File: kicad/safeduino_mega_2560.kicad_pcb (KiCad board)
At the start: 4 copper layers, 134.5 x 63.9 mm, 127 parts, among them X1 USB

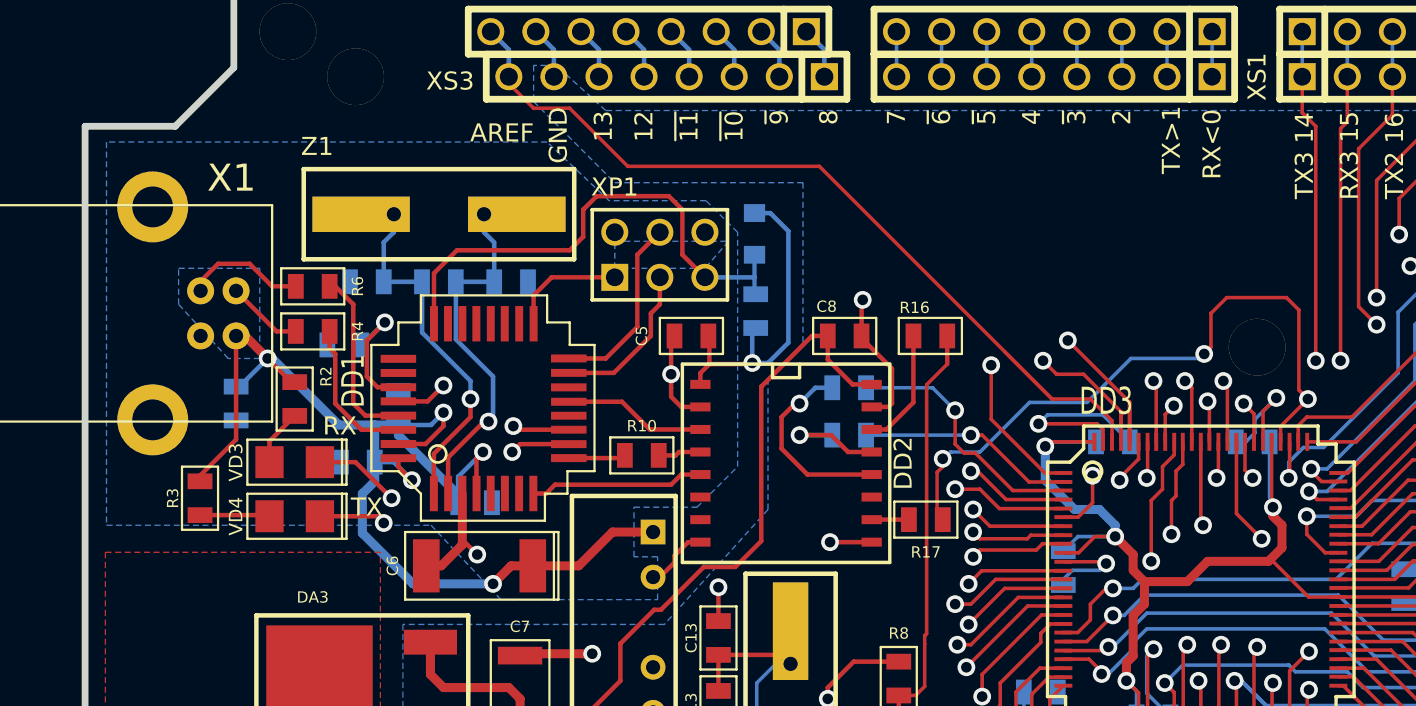
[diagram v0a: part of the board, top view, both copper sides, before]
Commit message: Исправил ошибку в подключении ADUM1301.
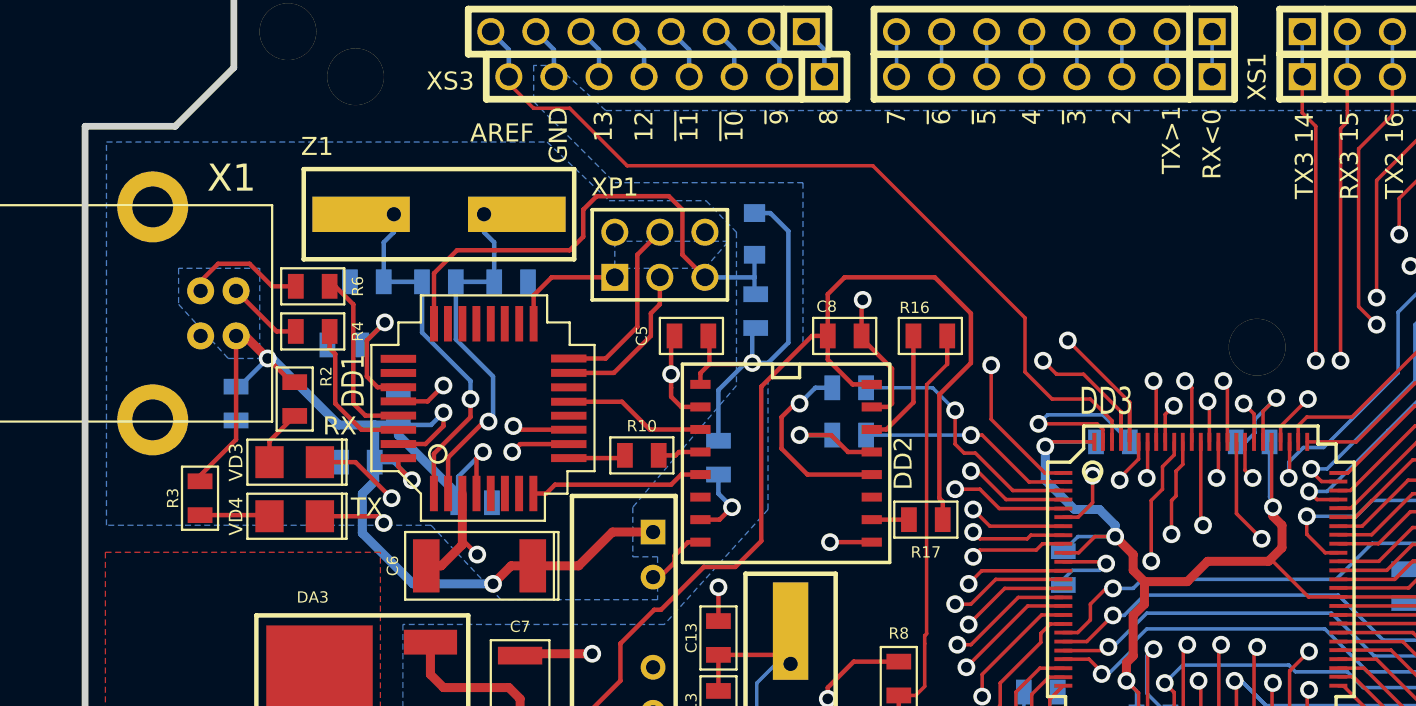
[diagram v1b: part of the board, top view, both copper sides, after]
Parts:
- added R19: 1к, SMD0805, B.Cu at (89.2, 118.1)
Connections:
- DD2 pad 7: (no net) -> N-0000037
- R17 pad 2: /PJ7 -> /MPU_VCC
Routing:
- net /PJ7: track 84.5 -> 50.2 mm, vias 4 -> 2
- net /MPU_VCC: track 434.4 -> 458.4 mm
- net /5V_USB: track 120.9 -> 126.3 mm
- net N-0000037: track 0.00 -> 4.22 mm, vias 0 -> 1
- net /AREF: track 50.2 -> 48.2 mm

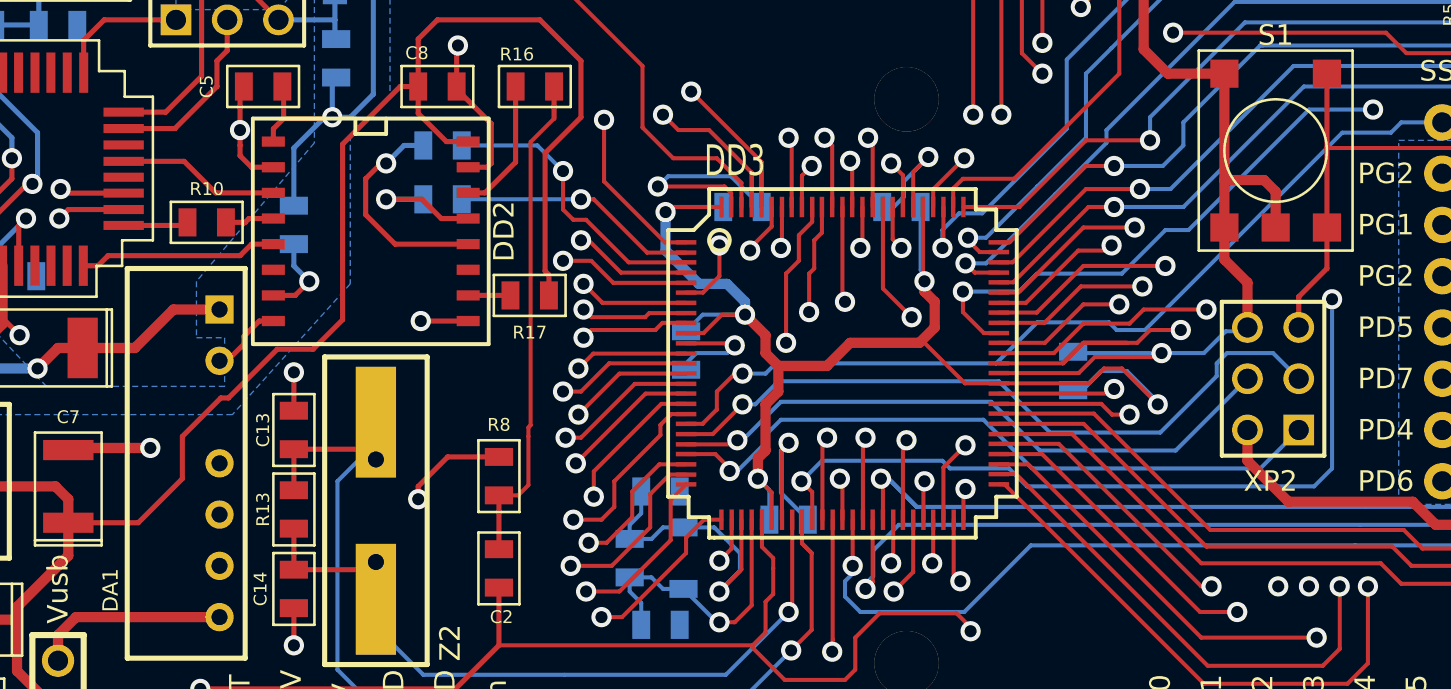
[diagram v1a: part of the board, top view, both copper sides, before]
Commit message: Исправил ошибку с сигналом RESER.
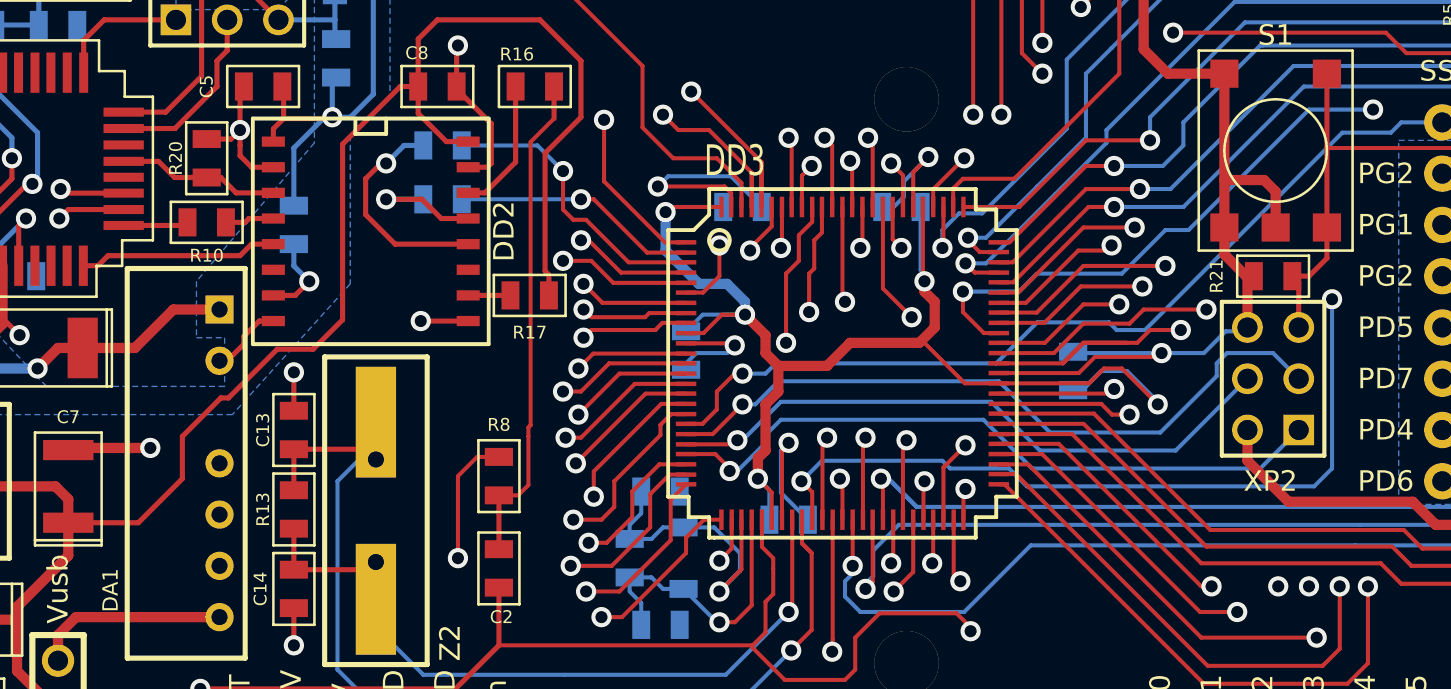
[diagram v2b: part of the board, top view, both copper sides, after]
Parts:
- added R20: 1к, SMD0805, F.Cu at (84.8, 114.8)
- added R21: 1М, SMD0805, F.Cu at (137.7, 120.7)
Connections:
- R8 pad 1: /GND_USB -> /GND
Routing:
- net /GND_USB: track 39.9 -> 23.0 mm, vias 4 -> 3
- net /GND: track 136.5 -> 143.7 mm, vias 14 -> 15
- net /RESET: track 116.1 -> 116.9 mm

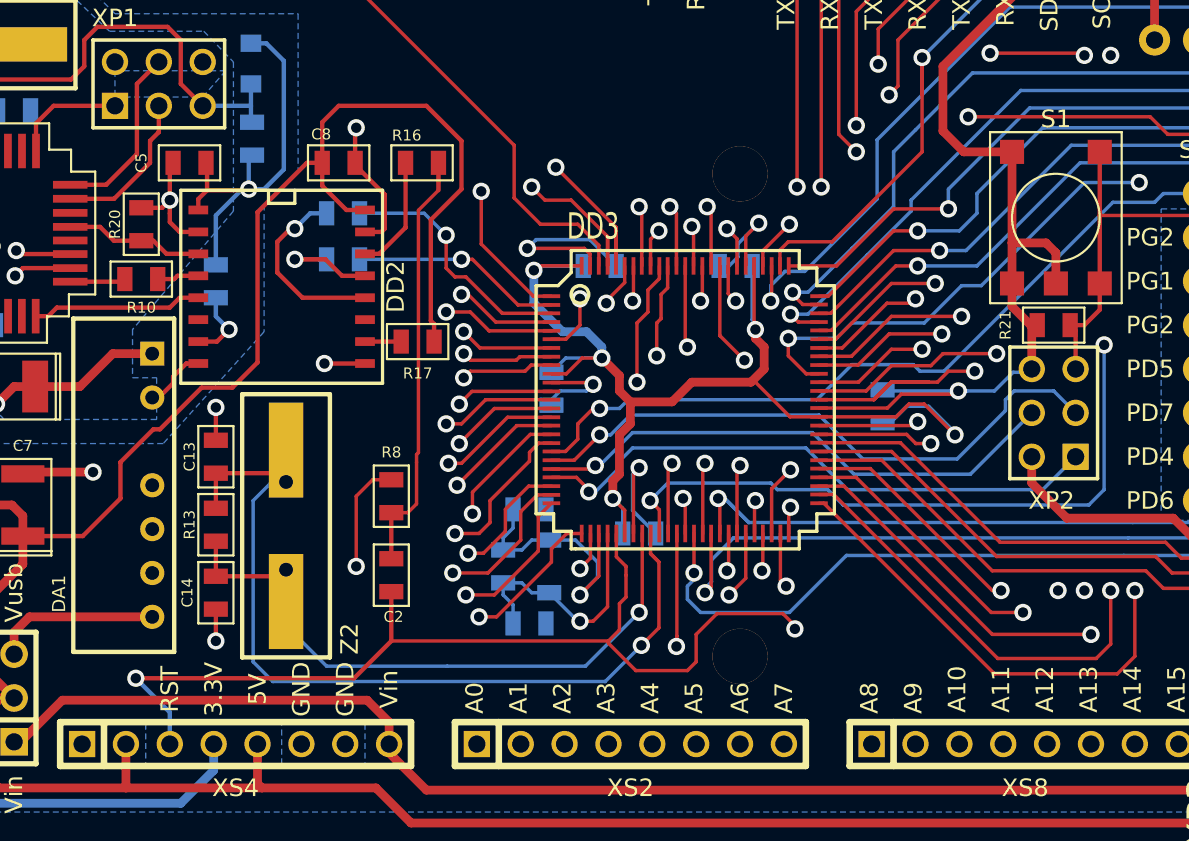
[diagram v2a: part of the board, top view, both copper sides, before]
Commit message: Услучшил разводку платы SafeDuino MEGA 2560.
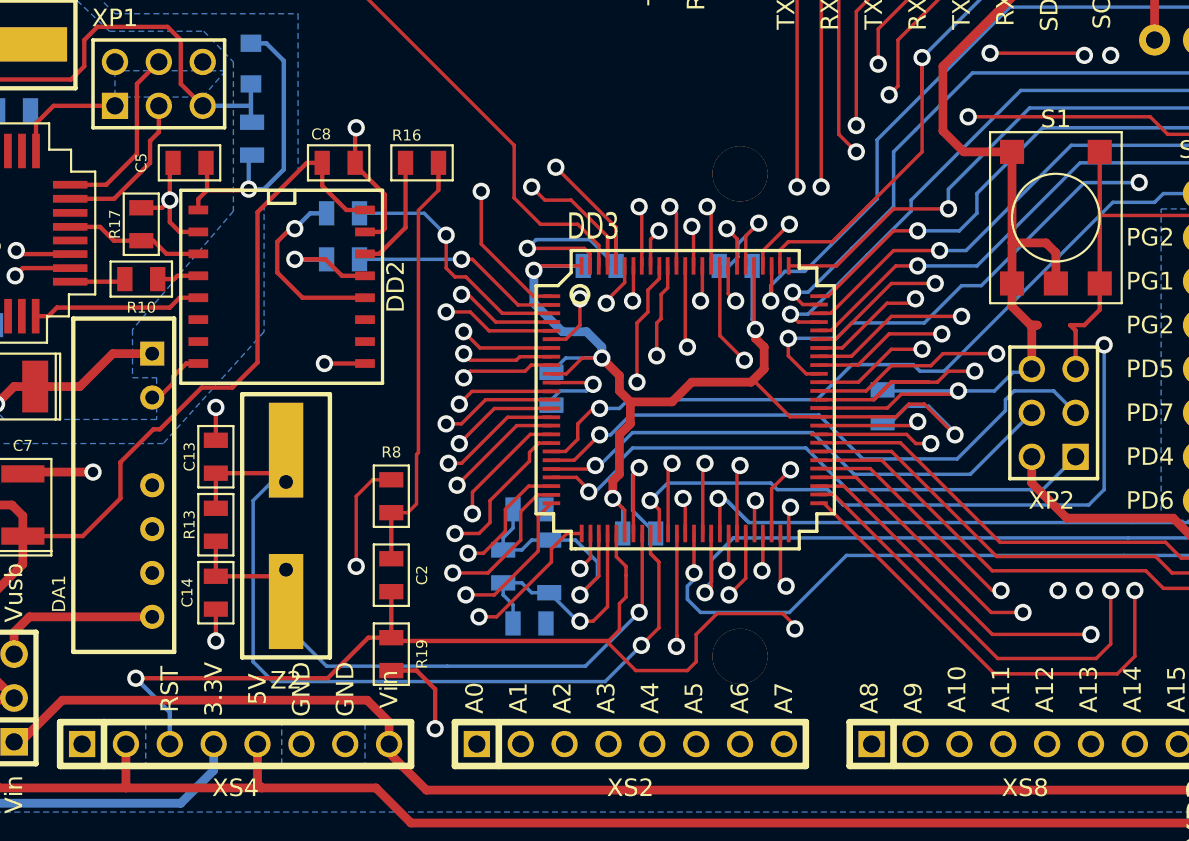
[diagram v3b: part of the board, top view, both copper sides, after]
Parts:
- removed the R17 at (100.8, 121.6)
- removed R21: 1М, SMD0805
- R19: value 1к -> 1М; moved to F.Cu
- moved R19 23.9 mm to (99.3, 139.7), turned to 90 degrees
- renumbered R20 to R17
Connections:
- DD2 pad 10: N-00000147 -> (no net)
- DD2 pad 7: N-0000048 -> (no net)
- R19 pad 1: /5V_USB -> /GND
- R19 pad 2: N-0000048 -> /RESET
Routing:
- net /MPU_VCC: track 458.4 -> 434.4 mm
- net /5V_USB: track 126.3 -> 120.9 mm
- net /GND: track 143.7 -> 149.0 mm, vias 15 -> 16
- net N-0000048: track 4.22 -> 0.00 mm, vias 1 -> 0
- net N-00000147: track 2.49 -> 0.00 mm

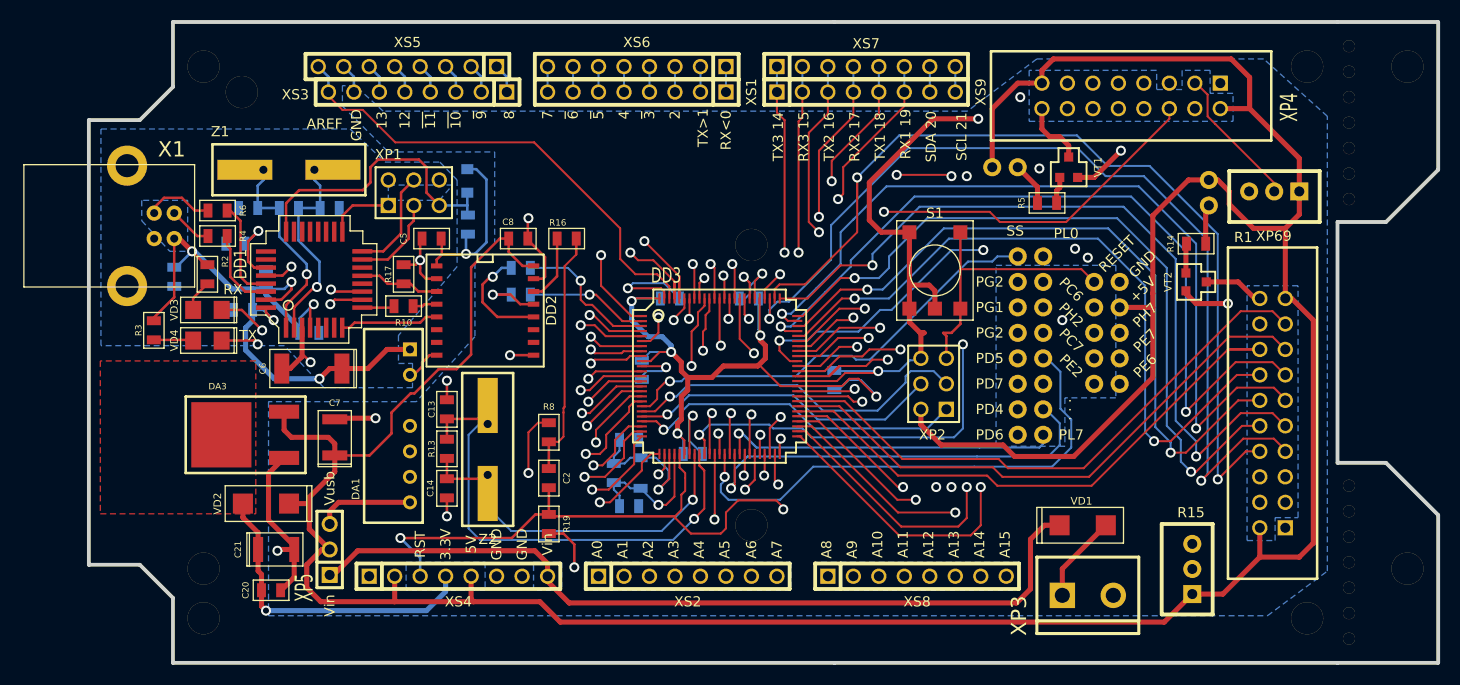
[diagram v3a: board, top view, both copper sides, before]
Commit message: Поправил ошибку с перевёрнутым разъёмом.
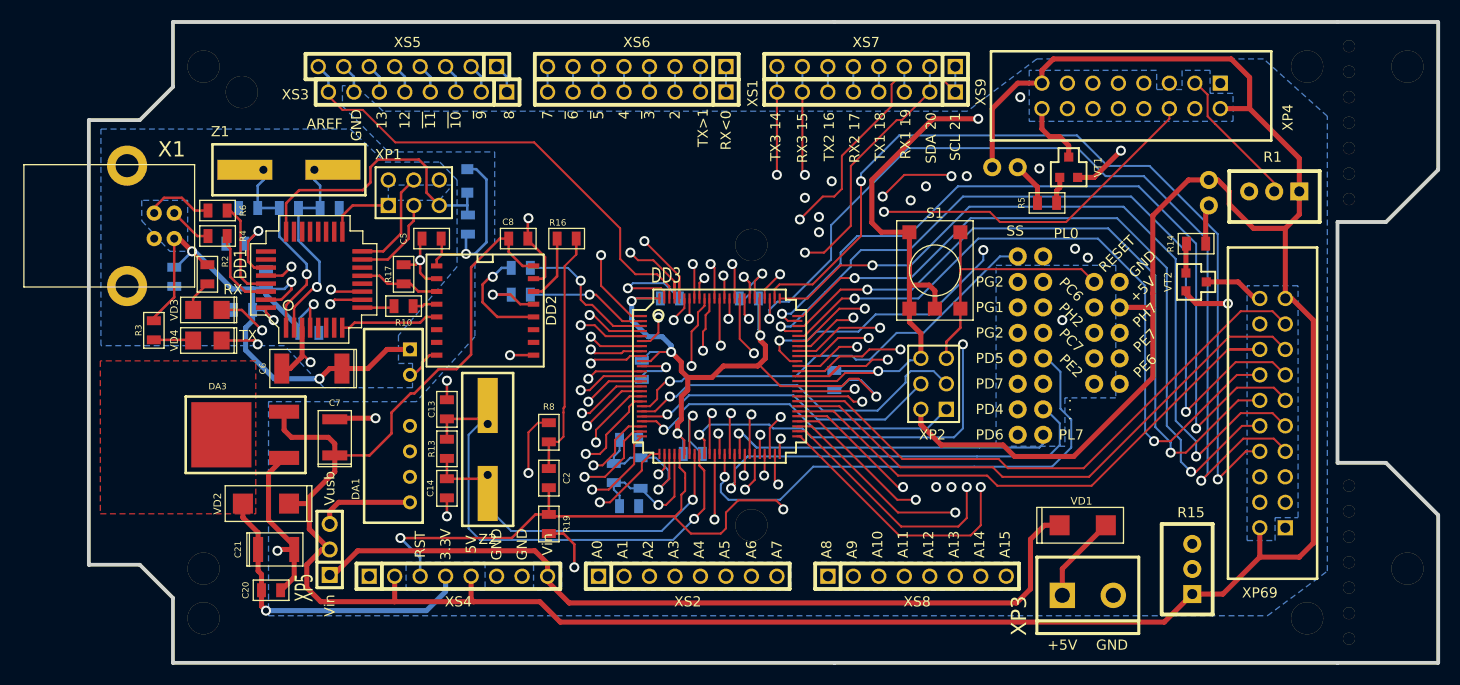
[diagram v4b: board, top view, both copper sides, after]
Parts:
- turned XS7 to 180 degrees
- turned XS9 to 180 degrees
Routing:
- net /PJ1: track 41.6 -> 61.6 mm, vias 1 -> 3
- net /PD0: track 46.4 -> 58.2 mm
- net /PJ0: track 46.4 -> 55.3 mm, vias 1 -> 3
- net /PD1: track 41.3 -> 47.5 mm
- net /PH1: track 59.9 -> 55.2 mm
- net /PD2: track 50.7 -> 53.1 mm
- net /PA1: track 90.7 -> 89.0 mm
- net /PA4: track 82.2 -> 81.1 mm
- net /PH0: track 55.4 -> 54.3 mm
- net /PD3: track 42.8 -> 43.8 mm
- net /GND: track 149.0 -> 148.0 mm
- net /RESET: track 116.9 -> 116.1 mm
- net /PA2: track 77.8 -> 77.1 mm
- net /PA3: track 73.7 -> 73.0 mm
- net /PJ3: track 52.2 -> 52.8 mm

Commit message: Исправил неточности в схеме.
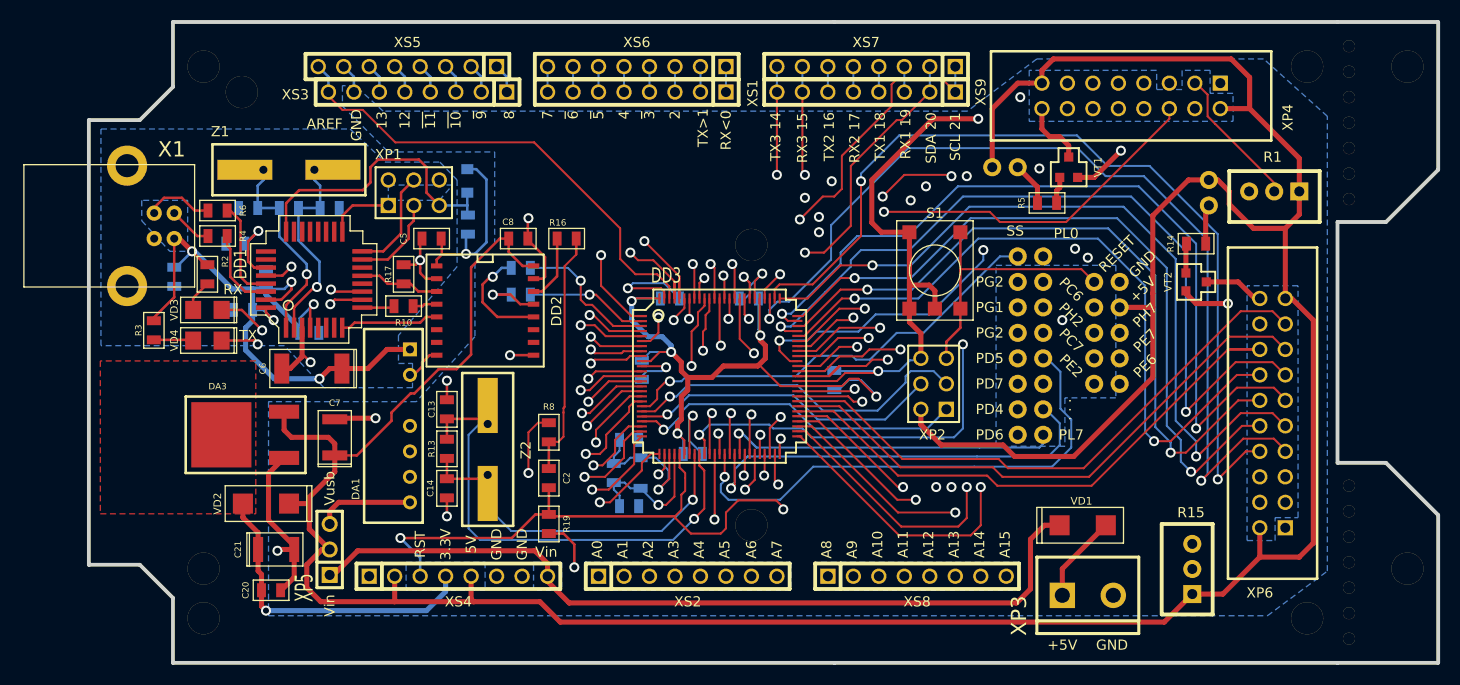
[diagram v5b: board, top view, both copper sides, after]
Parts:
- C22, C23: value 12.5п -> 12п
- R19: value 1М -> 1M
- XS4: value PBS-6 -> PBS-8
- renumbered XP6 to XP16, XP69 to XP6
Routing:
- net /PJ4: track 62.0 -> 58.0 mm
- net /MPU_VCC: track 434.4 -> 431.2 mm
- net /PJ5: track 41.1 -> 40.1 mm
- net /PG2: track 40.6 -> 40.0 mm
